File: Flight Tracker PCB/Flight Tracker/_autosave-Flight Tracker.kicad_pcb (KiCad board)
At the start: 2 copper layers, 53 parts, among them J1 Screw_Terminal_01x02, J2 Conn_01x02, J3 Conn_01x02, J4 Conn_02x03_Odd_Even, J5 Conn_01x02, Q1 FQP47P06, Q2 BSS138, Q3 BSS138, Q4 BSS138, Q5 BSS138, Q6 BSS138, Q7 BSS138, Q8 BSS138, Q9 BSS138, U1 NTX2, U2 UBlox_MAX8, U3 BH1750, U4 MPU_9250, U5 ML8511, U6 BMP280, U7 SMA_5pin, U8 UM232R

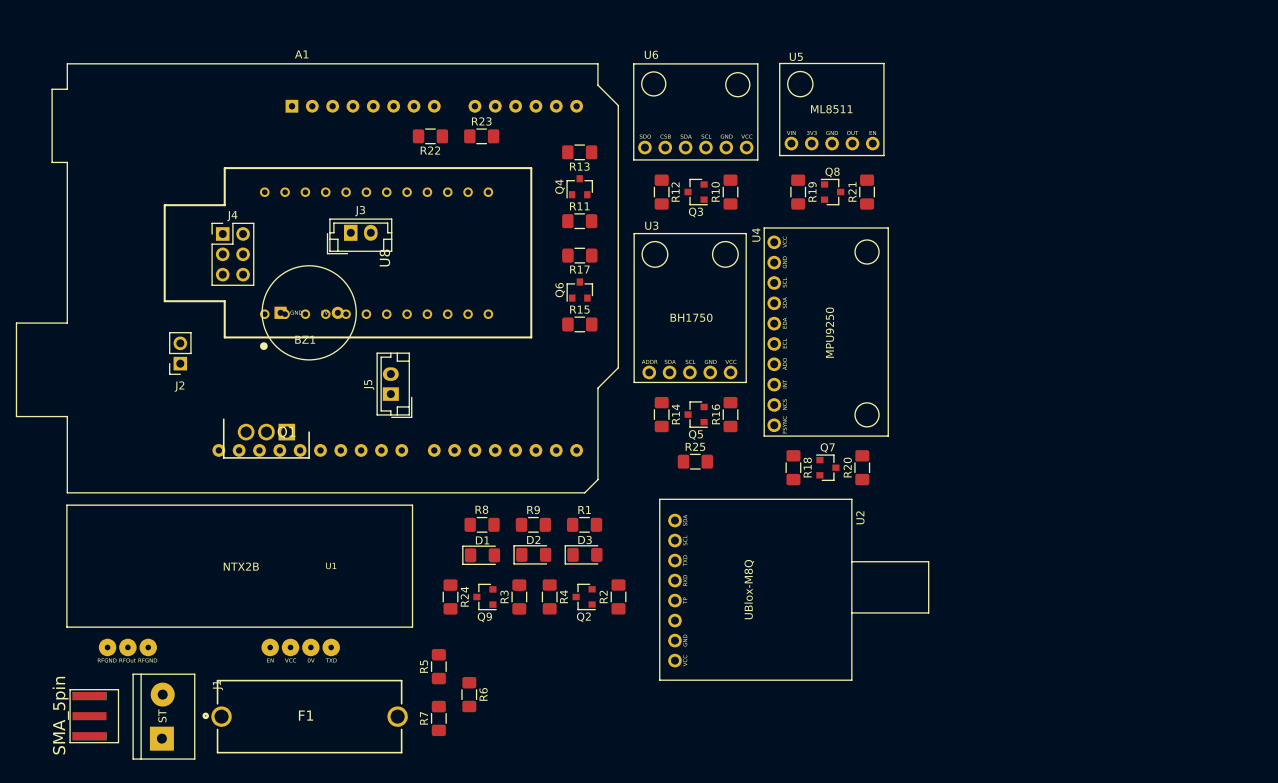
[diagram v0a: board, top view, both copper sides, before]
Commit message: created draft pcb, decided that removing the um232r footprint is required to make the pcb look nicer
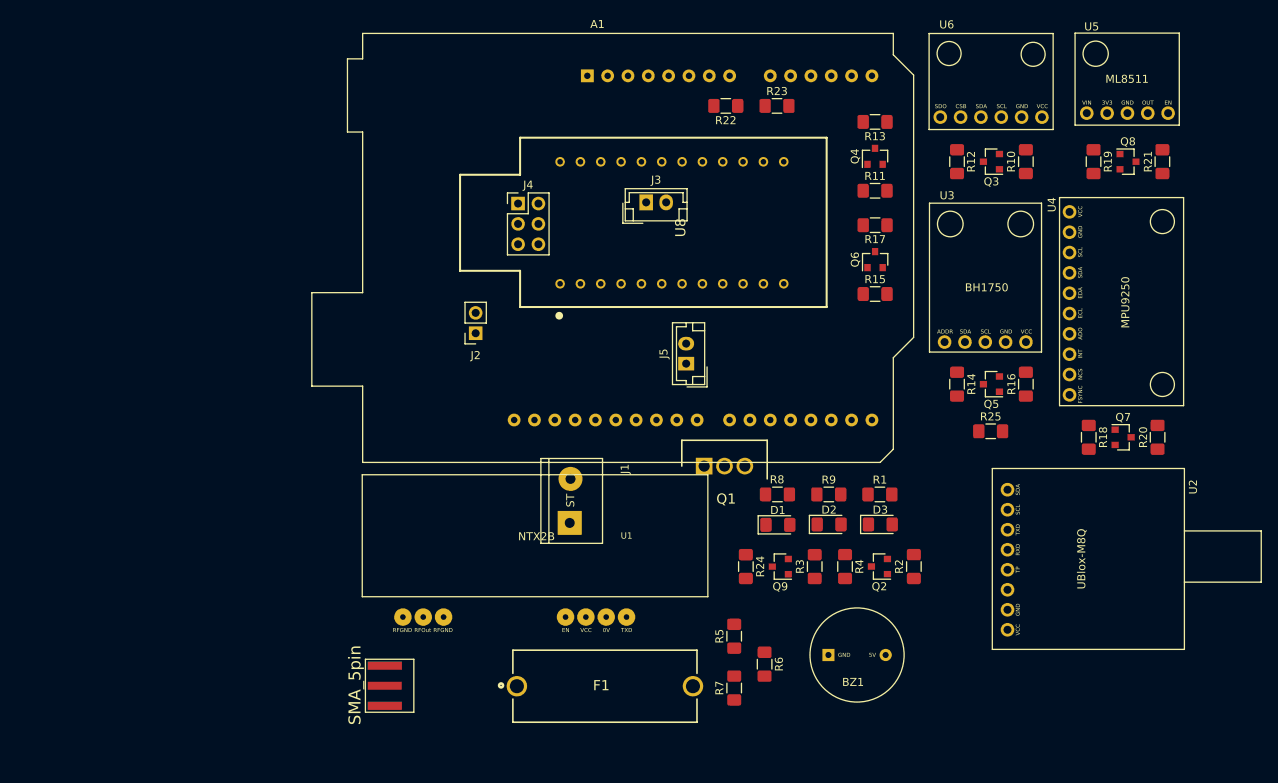
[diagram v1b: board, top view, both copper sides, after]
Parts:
- moved BZ1 80.7 mm to (153.4, 116.5)
- moved J1 57.6 mm to (117.7, 97.2)
- moved Q1 52.3 mm to (134.3, 92.9), turned to 0 degrees
- moved U2 41.7 mm to (181.7, 104.4)
- moved A1 37.1 mm to (119.8, 41.5)
- moved D3 37.1 mm to (156.4, 100.2)
- moved F1 37.1 mm to (122.0, 120.4)
- moved Q2 37.1 mm to (156.2, 105.5)
- moved Q3 37.1 mm to (170.2, 54.9)
- moved Q5 37.1 mm to (170.2, 82.7)
- moved Q6 37.1 mm to (155.7, 67.1)
- moved Q8 37.1 mm to (187.3, 54.9)
- moved R10 37.1 mm to (174.5, 54.9)
- moved R15 37.1 mm to (155.7, 71.4)
- moved R16 37.1 mm to (174.5, 82.7)
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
